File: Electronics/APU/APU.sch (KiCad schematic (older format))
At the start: 12 parts, among them J30 Screw_Terminal_01x10, J31 Screw_Terminal_01x10, J32 Screw_Terminal_01x10, U41 74HC165, U42 ProMicro, U43 74HC4051, U44 74HC4051

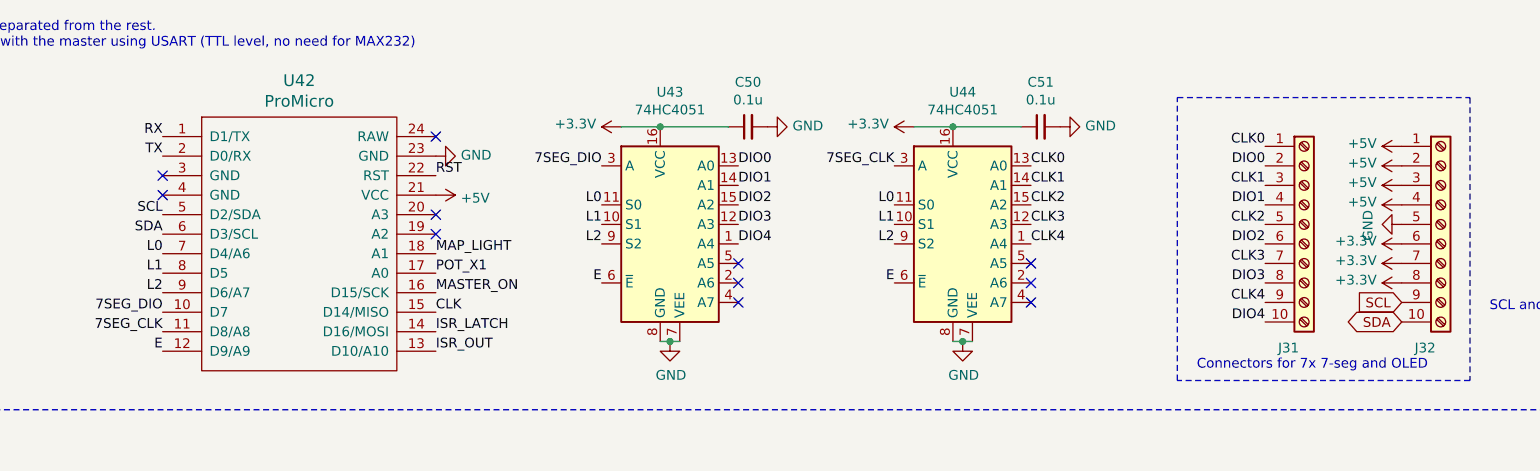
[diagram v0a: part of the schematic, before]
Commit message: Electrnonics - Change label on pedestral after separation
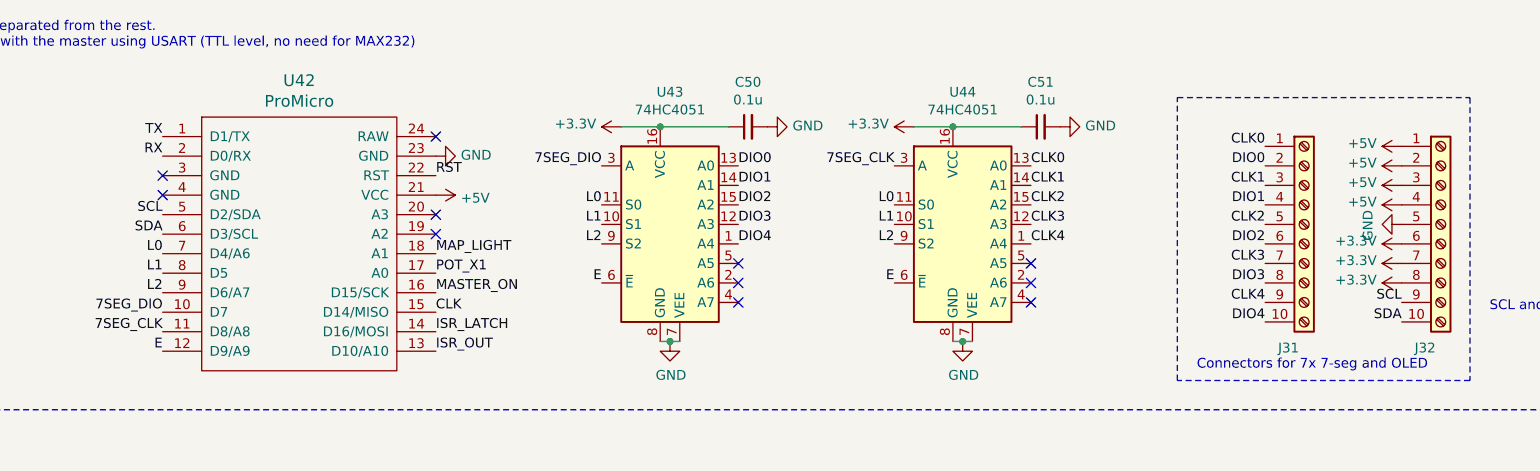
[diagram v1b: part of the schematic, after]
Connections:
- net RX: now also U42.2 (D0/RX); no longer U42.1 (D1/TX)
- net TX: now also U42.1 (D1/TX); no longer U42.2 (D0/RX)
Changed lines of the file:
@@
 EESchema Schematic File Version 4
-LIBS:CitationX_cockpit-cache
 EELAYER 26 0
 EELAYER END
 $Descr A4 11693 8268
 encoding utf-8
-Sheet 6 10
+Sheet 1 1
 Title ""
 Date ""
@@
 AR Path="/5DB6029E/5DC01A64" Ref="J?"  Part="1"
 AR Path="/5DC174D6/5DC01A64" Ref="J32"  Part="1"
+AR Path="/5DC01A64" Ref="J32"  Part="1"
 F 0 "J32" H 8620 1017 50  0000 C CNN
 F 1 "Screw_Terminal_01x10" H 8620 1016 50  0001 C CNN
@@
 	0    -1   -1   0
 $EndComp
-Text GLabel 8500 2050 0    50   Input ~ 0
-SCL
-Text GLabel 8500 2150 0    50   BiDi ~ 0
-SDA
 $Comp
 L power:+5V #PWR?
@@
 	0    -1   -1   0
 $EndComp
+Text Label 2150 1300 2    50   ~ 0
+RX
 Text Label 2150 1200 2    50   ~ 0
-RX
-Text Label 2150 1300 2    50   ~ 0
 TX
 Text Label 8000 3550 2    50   ~ 0
@@
 Text Label 2150 1700 2    50   ~ 0
 SDA
+Text Label 8500 2050 2    50   ~ 0
+SCL
+Text Label 8500 2150 2    50   ~ 0
+SDA
 $EndSCHEMATC

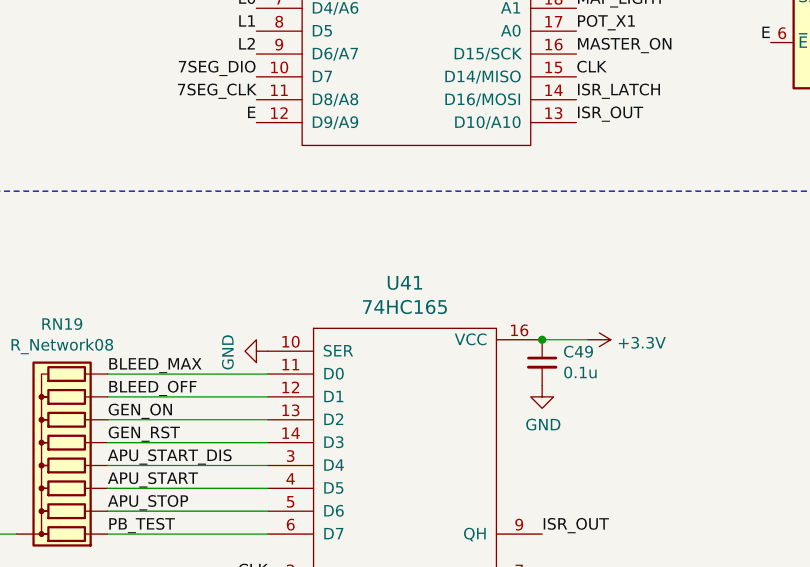
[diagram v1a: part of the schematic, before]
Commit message: Electronics - Footprints and LCSC for APU and Pedestral
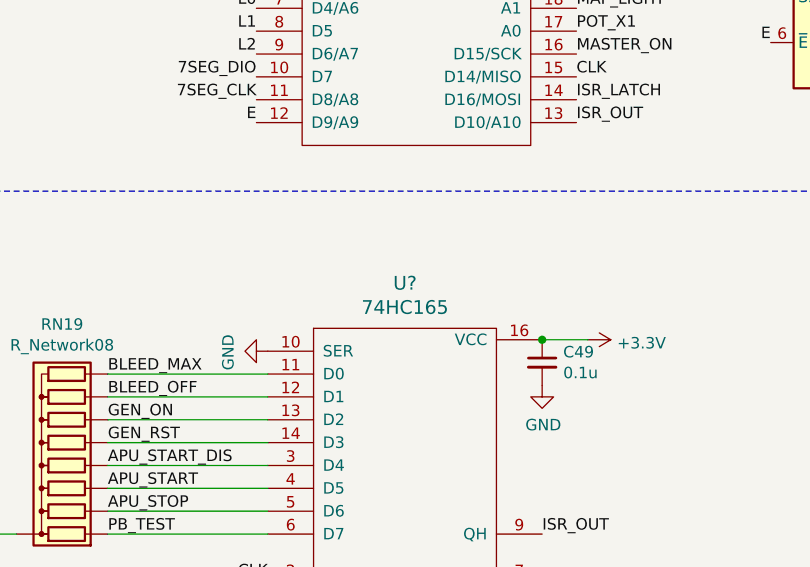
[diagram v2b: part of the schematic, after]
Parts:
- U41: footprint (none) -> Package_SO:SOIC-16_3.9x9.9mm_P1.27mm; LCSC (none) -> C5613
- U42: footprint (none) -> promicro:ProMicro
- U43, U44: footprint (none) -> Package_SO:HTSSOP-16-1EP_4.4x5mm_P0.65mm_EP3.4x5mm; LCSC (none) -> C5645
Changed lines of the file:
@@
 EESchema Schematic File Version 4
+LIBS:APU-cache
 EELAYER 26 0
 EELAYER END
@@
 AR Path="/5DB6029E/5DC019C4" Ref="U?"  Part="1"
 AR Path="/5DC174D6/5DC019C4" Ref="U42"  Part="1"
+AR Path="/5DC019C4" Ref="U42"  Part="1"
 F 0 "U42" H 2850 2987 60  0000 C CNN
 F 1 "ProMicro" H 2850 2881 60  0000 C CNN
-F 2 "" H 2950 900 60  0000 C CNN
+F 2 "promicro:ProMicro" H 2950 900 60  0001 C CNN
 F 3 "" H 2950 900 60  0000 C CNN
 	1    2850 1950
@@
 AR Path="/5DB6029E/5DC019EB" Ref="U?"  Part="1"
 AR Path="/5DC174D6/5DC019EB" Ref="U43"  Part="1"
+AR Path="/5DC019EB" Ref="U43"  Part="1"
 F 0 "U43" H 4750 2328 50  0000 C CNN
 F 1 "74HC4051" H 4750 2237 50  0000 C CNN
-F 2 "" H 4700 1250 50  0001 C CNN
+F 2 "Package_SO:HTSSOP-16-1EP_4.4x5mm_P0.65mm_EP3.4x5mm" H 4700 1250 50  0001 C CNN
 F 3 "http://www.ti.com/lit/ds/symlink/cd74hc4051.pdf" H 4700 1250 50  0001 C CNN
+F 4 "C5645" H 4700 1650 50  0001 C CNN "LCSC"
 	1    4700 1650
 	1    0    0    -1
@@
 AR Path="/5DB6029E/5DC01A1E" Ref="U?"  Part="1"
 AR Path="/5DC174D6/5DC01A1E" Ref="U44"  Part="1"
+AR Path="/5DC01A1E" Ref="U44"  Part="1"
 F 0 "U44" H 6250 2328 50  0000 C CNN
 F 1 "74HC4051" H 6250 2237 50  0000 C CNN
-F 2 "" H 6200 1250 50  0001 C CNN
+F 2 "Package_SO:HTSSOP-16-1EP_4.4x5mm_P0.65mm_EP3.4x5mm" H 6200 1250 50  0001 C CNN
 F 3 "http://www.ti.com/lit/ds/symlink/cd74hc4051.pdf" H 6200 1250 50  0001 C CNN
+F 4 "C5645" H 6200 1650 50  0001 C CNN "LCSC"
 	1    6200 1650
 	1    0    0    -1
@@
 AR Path="/5DC174D4/5DC04FDB" Ref="U?"  Part="1"
 AR Path="/5DC174D6/5DC04FDB" Ref="U41"  Part="1"
-F 0 "U41" H 2800 4797 60  0000 C CNN
+F 0 "U?" H 2800 4797 60  0000 C CNN
 F 1 "74HC165" H 2800 4691 60  0000 C CNN
-F 2 "" H 4990 2680 60  0001 C CNN
+F 2 "Package_SO:SOIC-16_3.9x9.9mm_P1.27mm" H 4990 2680 60  0001 C CNN
 F 3 "" H 4990 2680 60  0001 C CNN
+F 4 "C5613" H 2800 3900 50  0001 C CNN "LCSC"
 	1    2800 3900
 	1    0    0    -1
